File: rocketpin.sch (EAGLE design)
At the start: 5 parts

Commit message: v2, ordered from seeed studio spring 2017
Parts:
- R1: value (none) -> 47R
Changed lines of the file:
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@@
 <part name="FLASH" library="led" deviceset="LED" device="5MM"/>
 <part name="LED" library="led" deviceset="LED" device="5MM"/>
-<part name="R1" library="resistor" deviceset="R-US_" device="0207/10"/>
+<part name="R1" library="resistor" deviceset="R-US_" device="0207/10" value="47R"/>
 <part name="R2" library="resistor" deviceset="R-US_" device="0207/10" value="47R"/>
 <part name="U$2" library="battery" deviceset="CR2032-GK" device=""/>

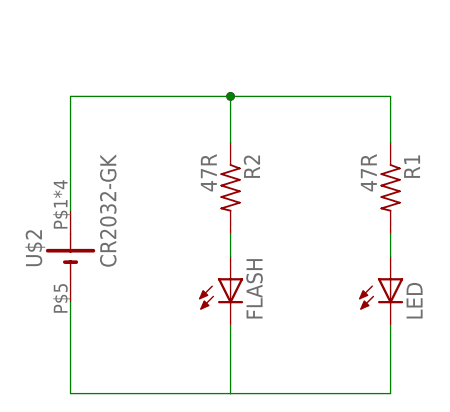
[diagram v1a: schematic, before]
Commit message: changed size to add button
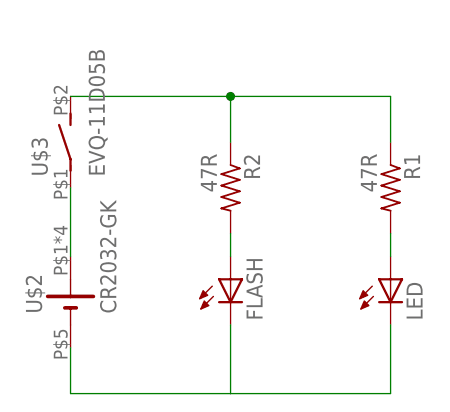
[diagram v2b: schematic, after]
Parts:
- added U$3: EVQ-11D05B, switch:EVQ-11D05B
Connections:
- new net N$6: U$2.+, U$3.P
- net N$1: now also U$3.S; no longer U$2.+
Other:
- moved on the sheet: U$2
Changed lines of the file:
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@@
 <part name="R2" library="resistor" deviceset="R-US_" device="0207/10" value="47R"/>
 <part name="U$2" library="battery" deviceset="CR2032-GK" device=""/>
+<part name="U$3" library="switch" deviceset="EVQ-11D05B" device=""/>
 </parts>
 <sheets>
@@
 <instance part="R1" gate="G$1" x="55.88" y="68.58" rot="R270"/>
 <instance part="R2" gate="G$1" x="38.1" y="68.58" rot="R270"/>
-<instance part="U$2" gate="G$1" x="20.32" y="60.96" rot="R90"/>
+<instance part="U$2" gate="G$1" x="20.32" y="55.88" rot="R90"/>
+<instance part="U$3" gate="G$1" x="20.32" y="73.66"/>
 </instances>
 <busses>
@@
 <pinref part="R2" gate="G$1" pin="1"/>
 <wire x1="38.1" y1="73.66" x2="38.1" y2="78.74" width="0.1524" layer="91"/>
-<pinref part="U$2" gate="G$1" pin="+"/>
-<wire x1="20.32" y1="66.04" x2="20.32" y2="78.74" width="0.1524" layer="91"/>
 <wire x1="20.32" y1="78.74" x2="38.1" y2="78.74" width="0.1524" layer="91"/>
 <pinref part="R1" gate="G$1" pin="1"/>
@@
 <wire x1="55.88" y1="78.74" x2="55.88" y2="73.66" width="0.1524" layer="91"/>
 <junction x="38.1" y="78.74"/>
+<pinref part="U$3" gate="G$1" pin="S"/>
 </segment>
 </net>
@@
 <pinref part="FLASH" gate="G$1" pin="C"/>
 <wire x1="38.1" y1="53.34" x2="38.1" y2="45.72" width="0.1524" layer="91"/>
-<wire x1="20.32" y1="55.88" x2="20.32" y2="45.72" width="0.1524" layer="91"/>
+<wire x1="20.32" y1="50.8" x2="20.32" y2="45.72" width="0.1524" layer="91"/>
 <pinref part="U$2" gate="G$1" pin="-"/>
 <wire x1="38.1" y1="45.72" x2="20.32" y2="45.72" width="0.1524" layer="91"/>
@@
 </segment>
 </net>
+<net name="N$6" class="0">
+<segment>
+<pinref part="U$2" gate="G$1" pin="+"/>
+<pinref part="U$3" gate="G$1" pin="P"/>
+<wire x1="20.32" y1="60.96" x2="20.32" y2="68.58" width="0.1524" layer="91"/>
+</segment>
+</net>
